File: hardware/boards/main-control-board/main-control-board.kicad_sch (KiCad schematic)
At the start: 10 parts, among them J1 Conn_MAX98357, J2 Conn_OLED, J3 Conn_PCA9685_1, J4 Conn_PCA9685_2, J5 Conn_ESP32_R, J6 Conn_ESP32_L, J7 Conn_USB

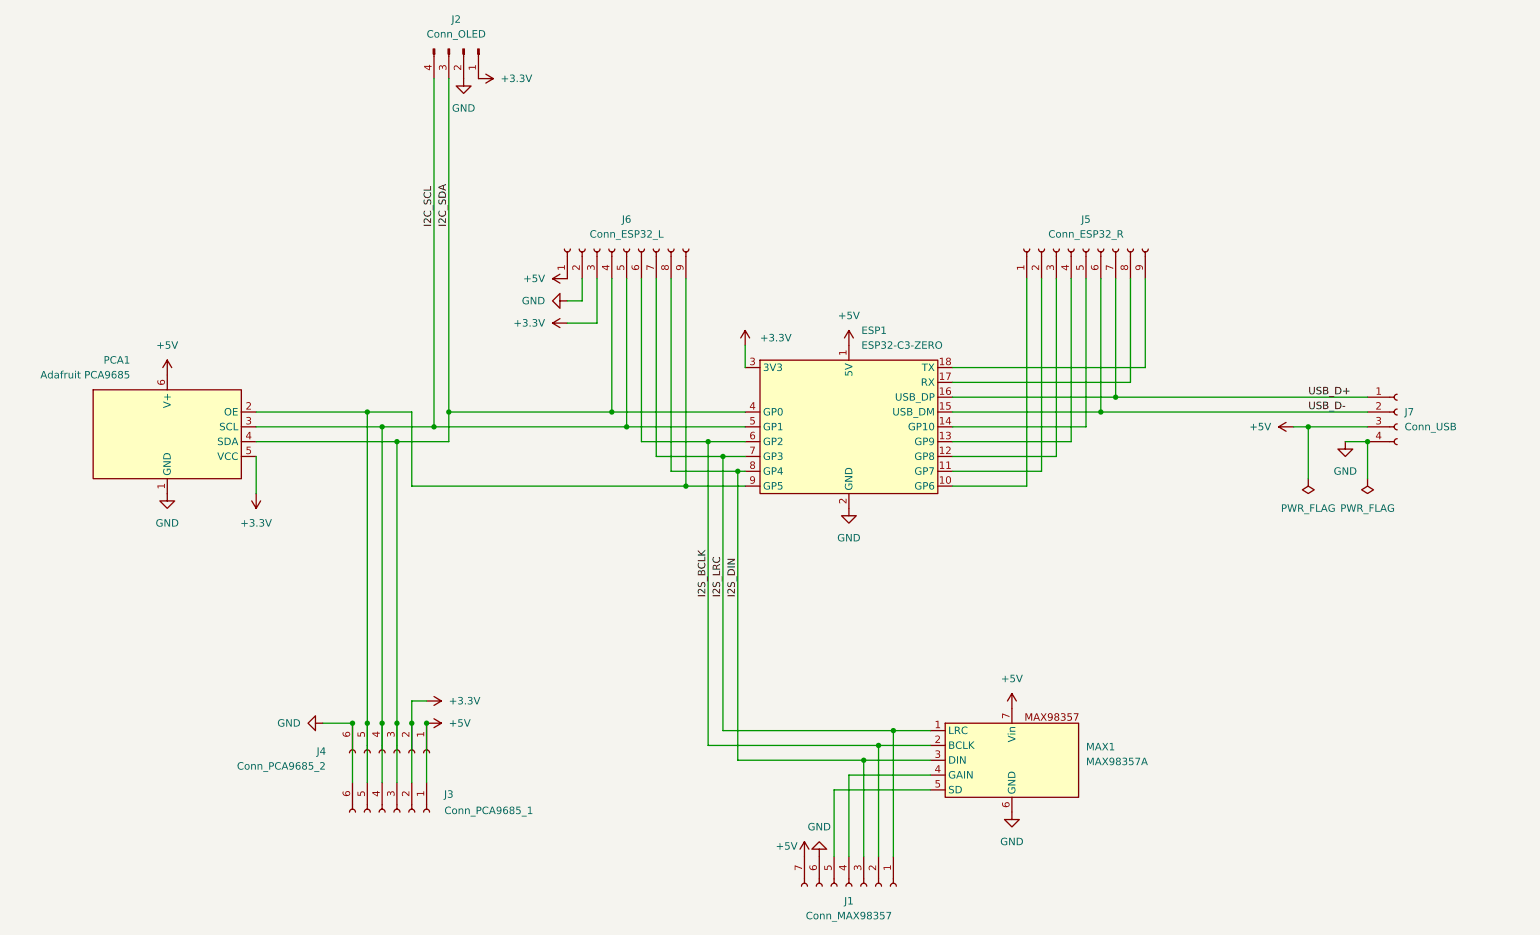
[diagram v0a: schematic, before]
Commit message: feat(pcb): design integrated PCB for Tiny Engineer electronics (#46, #10)
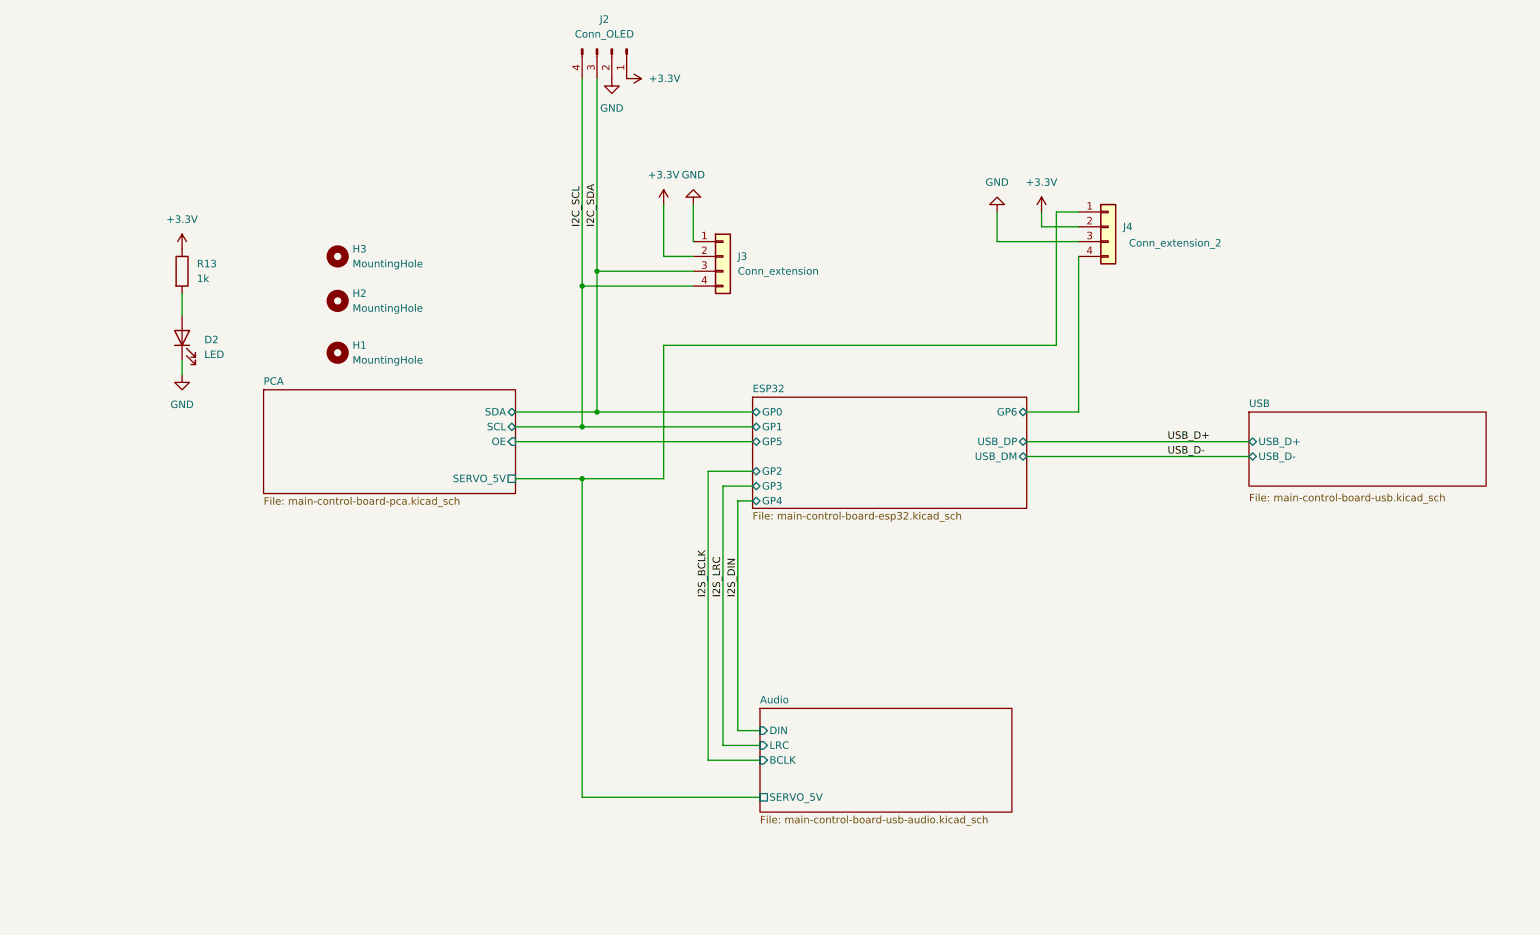
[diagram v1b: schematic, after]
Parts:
- removed ESP1: ESP32-C3-ZERO, TinyEngineerModules:ESP32_C3_Zero_Dev_Board, symbol TinyEngineerModules:ESP32_C3_Zero_Dev_Board
- removed J1: Conn_MAX98357, Connector_PinSocket_2.54mm:PinSocket_1x07_P2.54mm_Vertical, symbol Connector:Conn_01x07_Socket
- removed J3: Conn_PCA9685_1, Connector_PinSocket_2.54mm:PinSocket_1x06_P2.54mm_Vertical, symbol Connector:Conn_01x06_Socket
- removed J4: Conn_PCA9685_2, Connector_PinSocket_2.54mm:PinSocket_1x06_P2.54mm_Vertical, symbol Connector:Conn_01x06_Socket
- removed J5: Conn_ESP32_R, Connector_PinSocket_2.54mm:PinSocket_1x09_P2.54mm_Vertical, symbol Connector:Conn_01x09_Socket
- removed J6: Conn_ESP32_L, Connector_PinSocket_2.54mm:PinSocket_1x09_P2.54mm_Vertical, symbol Connector:Conn_01x09_Socket
- removed J7: Conn_USB, Connector_PinSocket_2.54mm:PinSocket_1x04_P2.54mm_Vertical, symbol Connector:Conn_01x04_Socket
- removed MAX1: MAX98357A, symbol TinyEngineerModules:MAX98357_Module
- removed PCA1: Adafruit PCA9685, symbol TinyEngineerModules:Adafruit_PCA9685_Module
- added D2: LED, LED_SMD:LED_0603_1608Metric, symbol Device:LED
- added H1, H2, H3: MountingHole, MountingHole:MountingHole_2.2mm_M2, symbol Mechanical:MountingHole
- added J3: Conn_extension, Connector_JST:JST_SH_SM04B-SRSS-TB_1x04-1MP_P1.00mm_Horizontal, symbol Connector_Generic:Conn_01x04
- added J4: Conn_extension_2, Connector_PinHeader_2.54mm:PinHeader_1x04_P2.54mm_Vertical, symbol Connector_Generic:Conn_01x04
- added R13: 1k, Resistor_SMD:R_0603_1608Metric, symbol Device:R
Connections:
- net +3.3V: now also J3.2 (Pin_2), J4.2 (Pin_2), R13.1
- net GND: now also D2.1 (K), J3.1 (Pin_1), J4.3 (Pin_3)
- net I2C_SCL: now also J3.4 (Pin_4)
- net I2C_SDA: now also J3.3 (Pin_3)
- new net: D2.2 (A), R13.2
- new net Audio/SERVO_5V: J4.1 (Pin_1)
- new net ESP32/GP6: J4.4 (Pin_4)
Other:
- added sheet Audio (main-control-board-usb-audio.kicad_sch)
- added sheet ESP32 (main-control-board-esp32.kicad_sch)
- added sheet PCA (main-control-board-pca.kicad_sch)
- added sheet USB (main-control-board-usb.kicad_sch)
- moved on the sheet: J2
